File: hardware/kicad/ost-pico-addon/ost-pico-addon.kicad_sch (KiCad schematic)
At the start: 8 parts, among them J1 Conn_01x09_Male, J2 47219-2001, J3 buttons, J4 Conn_01x02_Pin, J5 Conn_01x07_Pin, U1 Pico

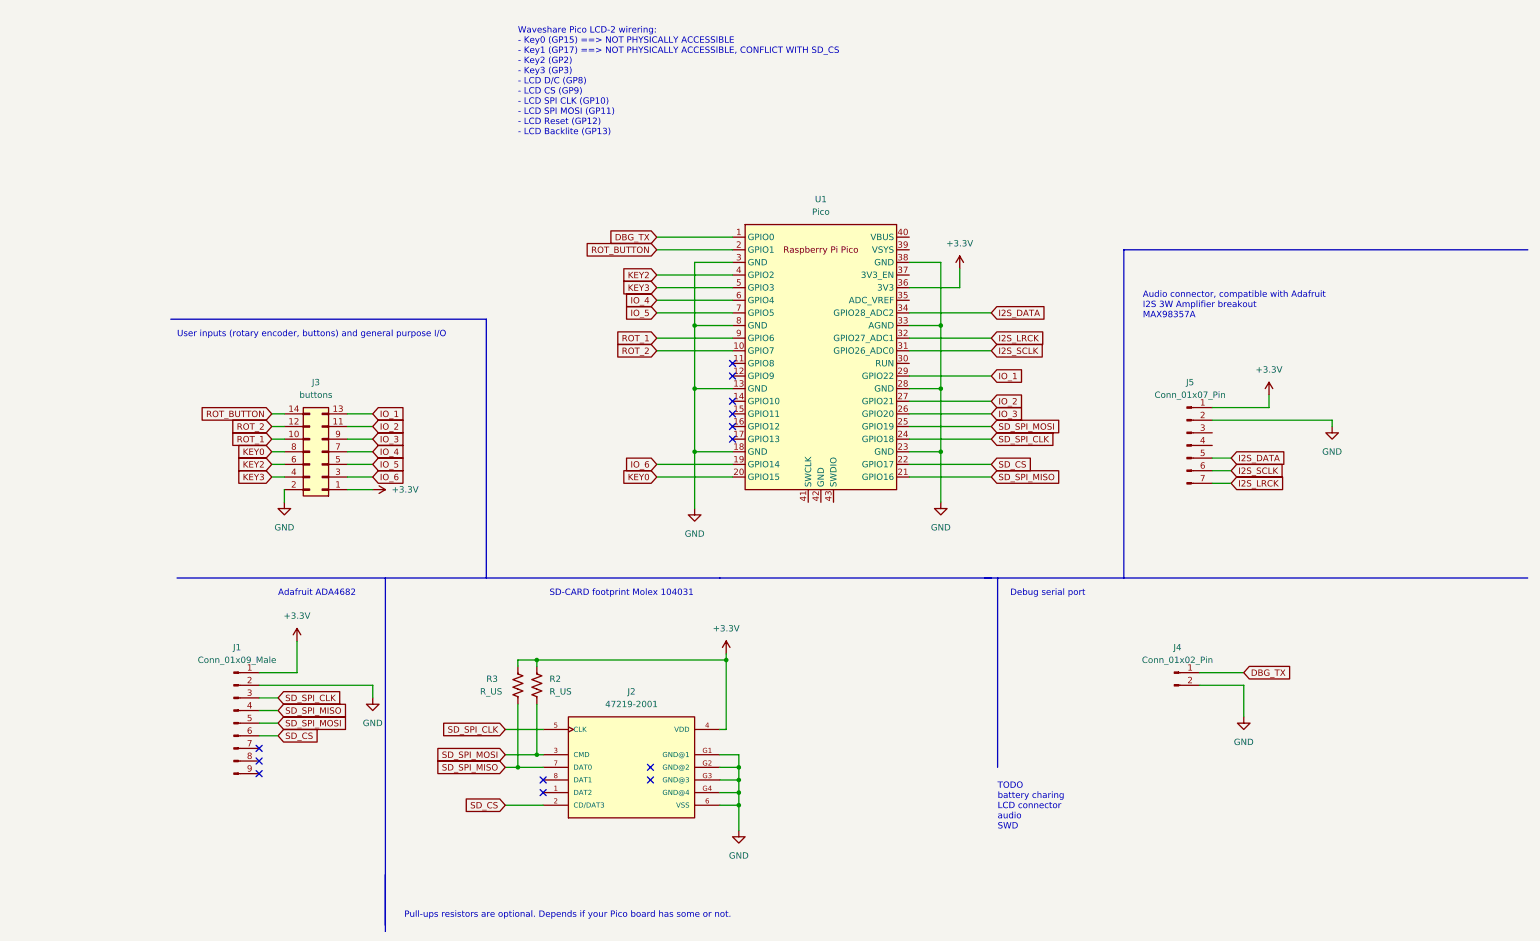
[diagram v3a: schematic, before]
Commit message: Pico audio with 3 audio chips (complex)
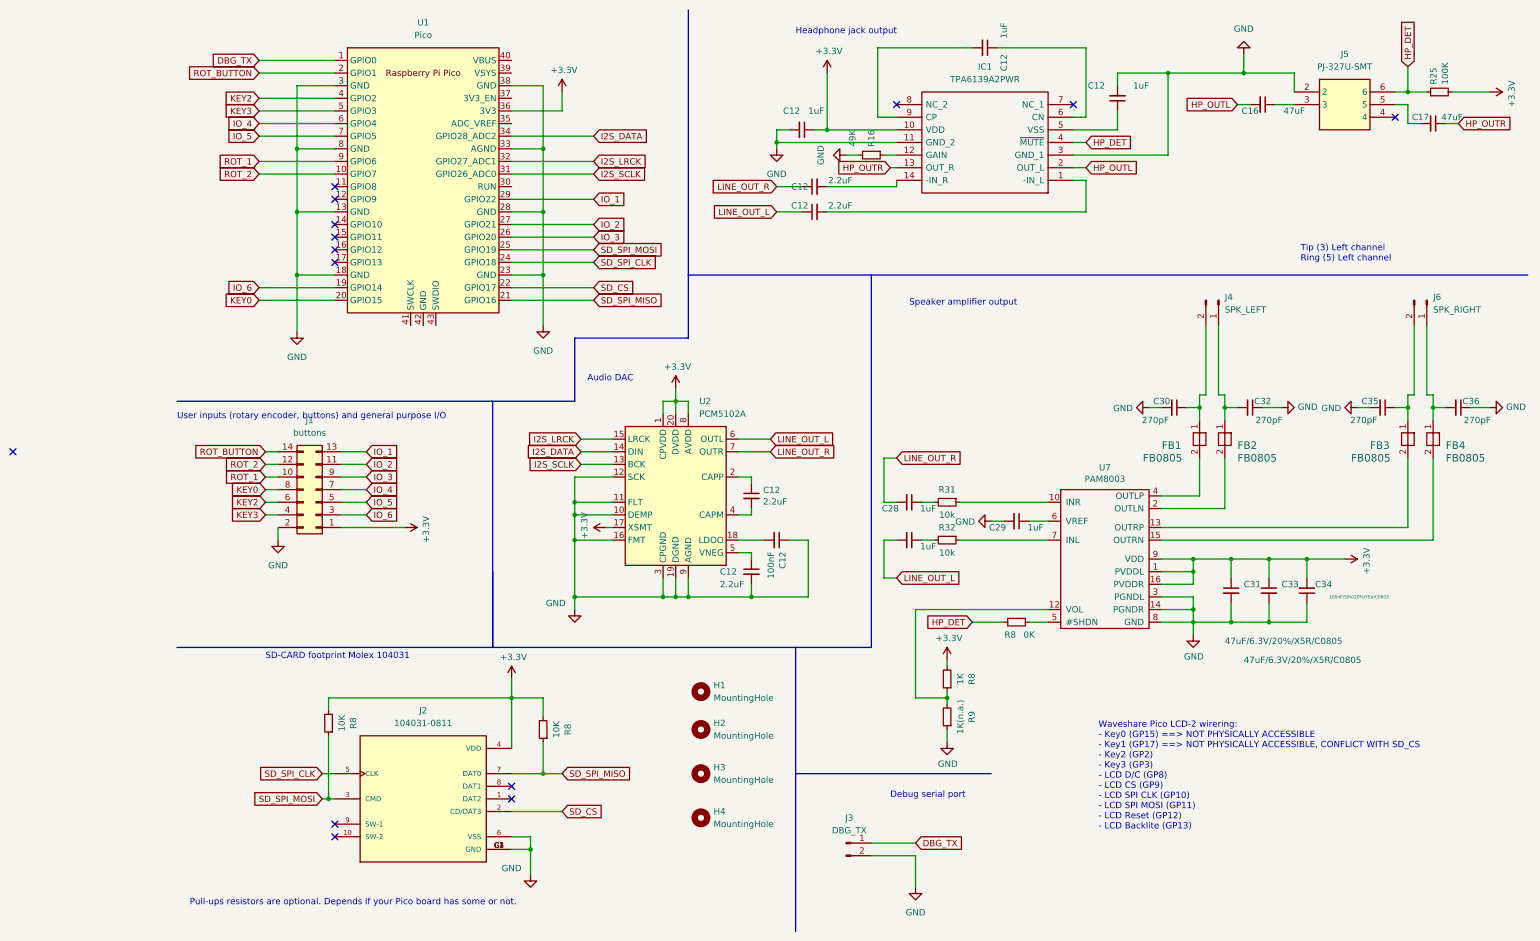
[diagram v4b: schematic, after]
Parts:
- removed J1: Conn_01x09_Male, Connector_PinHeader_2.54mm:PinHeader_1x09_P2.54mm_Vertical, symbol Connector:Conn_01x09_Male
- removed J2: 47219-2001, sdcard-libs:MOLEX_47219-2001, symbol sdcard-libs:47219-2001
- removed J5: Conn_01x07_Pin, Connector_PinHeader_2.54mm:PinHeader_1x07_P2.54mm_Vertical, symbol Connector:Conn_01x07_Pin
- removed R2, R3: R_US, Resistor_THT:R_Axial_DIN0207_L6.3mm_D2.5mm_P10.16mm_Horizontal, symbol Device:R_US
- added C12 (x4): 2.2uF, Capacitor_SMD:C_0805_2012Metric, symbol ESP32-ADF_Rev_C-rescue:C_Small-OLIMEX_RCL
- added C12 (x3), C27, C28, C29: 1uF, Capacitor_SMD:C_0805_2012Metric, symbol ESP32-ADF_Rev_C-rescue:C_Small-OLIMEX_RCL
- added C12: 100nF, Capacitor_SMD:C_0805_2012Metric, symbol ESP32-ADF_Rev_C-rescue:C_Small-OLIMEX_RCL
- added C16, C17: 47uF, Capacitor_SMD:C_0805_2012Metric, symbol ESP32-ADF_Rev_C-rescue:C_Small-OLIMEX_RCL
- added C30, C32, C35, C36: 270pF, Capacitor_SMD:C_0805_2012Metric, symbol ESP32-ADF_Rev_C-rescue:C_Small-OLIMEX_RCL
- added C31, C33: 47uF/6.3V/20%/X5R/C0805, Capacitor_SMD:C_0805_2012Metric, symbol ESP32-ADF_Rev_C-rescue:C-OLIMEX_RCL
- added C34: 100nF/50V/20%/Y5V/C0603, Capacitor_SMD:C_0805_2012Metric, symbol ESP32-ADF_Rev_C-rescue:C-OLIMEX_RCL
- added FB1, FB2, FB3, FB4: FB0805, Inductor_SMD:L_0805_2012Metric, symbol ESP32-ADF_Rev_C-rescue:FB0805-lz1ddd-ESP32-ADF_Rev_B-rescue
- added H1, H2, H3, H4: MountingHole, MountingHole:MountingHole_2.7mm_M2.5_ISO14580_Pad, symbol Mechanical:MountingHole
- added IC1: TPA6139A2PWR, audio:SOP65P640X120-14N, symbol TPA6139A2PWR:TPA6139A2PWR
- added J2: 104031-0811, sdcard-libs:MOLEX_104031-0811, symbol 104031-0811:104031-0811
- added J4: SPK_LEFT, Connector_PinHeader_2.54mm:PinHeader_1x02_P2.54mm_Vertical, symbol Connector:Conn_01x02_Pin
- added J5: PJ-327U-SMT, audio:PJ327USMT, symbol PJ-327U-SMT:PJ-327U-SMT
- added J6: SPK_RIGHT, Connector_PinHeader_2.54mm:PinHeader_1x02_P2.54mm_Vertical, symbol Connector:Conn_01x02_Pin
- added R16: 49K, Resistor_SMD:R_0805_2012Metric, symbol ESP32-ADF_Rev_C-rescue:R_Small-OLIMEX_RCL
- added R25: 100K, Resistor_SMD:R_0805_2012Metric, symbol ESP32-ADF_Rev_C-rescue:R_Small-OLIMEX_RCL
- added R31, R32: 10k, Resistor_SMD:R_0805_2012Metric, symbol ESP32-ADF_Rev_C-rescue:R_Small-OLIMEX_RCL
- added R8 (x2): 10K, Resistor_SMD:R_0805_2012Metric, symbol ESP32-ADF_Rev_C-rescue:R_Small-OLIMEX_RCL
- added R8: 0K, Resistor_SMD:R_0805_2012Metric, symbol ESP32-ADF_Rev_C-rescue:R_Small-OLIMEX_RCL
- added R8: 1K, Resistor_SMD:R_0805_2012Metric, symbol ESP32-ADF_Rev_C-rescue:R_Small-OLIMEX_RCL
- added R9: 1K(n.a.), Resistor_SMD:R_0805_2012Metric, symbol ESP32-ADF_Rev_C-rescue:R_Small-OLIMEX_RCL
- added U2: PCM5102A, Package_SO:TSSOP-20_4.4x6.5mm_P0.65mm, symbol Audio:PCM5102A
- added U7: PAM8003, audio:SO16, symbol ESP32-ADF_Rev_C-rescue:PAM8003-OLIMEX_IC-ESP32-ADF_Rev_B-rescue
- J3: renamed from J4; value Conn_01x02_Pin -> DBG_TX
- renumbered J3 to J1
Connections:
- net GND: now also C12.1, C12.2, C12.2, C12.2, C29.2, C30.2, C31.2, C32.1, C33.2, C34.1, C35.2, C36.1, IC1.11 (GND_2), IC1.3 (GND_1), J2.6 (VSS), J2.G1 (GND), J2.G2 (GND), J2.G3 (GND), J2.G4 (GND), J5.2, R16.2, R9.1, U2.10 (DEMP), U2.11 (FLT), U2.12 (SCK), U2.16 (FMT), U2.19 (DGND), U2.3 (CPGND), U2.9 (AGND), U7.14 (PGNDR), U7.3 (PGNDL), U7.8 (GND)
- net I2S_DATA: now also U2.14 (DIN)
- net I2S_LRCK: now also U2.15 (LRCK)
- net I2S_SCLK: now also U2.13 (BCK)
- net SD_CS: now also J2.2 (CD/DAT3)
- net SD_SPI_CLK: now also J2.5 (CLK)
- net SD_SPI_MISO: now also J2.7 (DAT0), R8.1
- net SD_SPI_MOSI: now also J2.3 (CMD), R8.1
- net +3.3V renamed +3V3
- net +3V3: now also C12.1, C31.1, C33.1, C34.2, IC1.10 (VDD), J2.4 (VDD), R25.2, R8.2, R8.2, R8.2, U2.1 (CPVDD), U2.17 (XSMT), U2.20 (DVDD), U2.8 (AVDD), U7.1 (PVDDL), U7.16 (PVDDR), U7.9 (VDD)
- new net: C12.2, IC1.14 (-IN_R)
- new net: C28.1, R32.2
- new net: C12.1, U2.5 (VNEG)
- new net: C36.2, FB4.1, J6.1 (Pin_1)
- new net: C35.1, FB3.1, J6.2 (Pin_2)
- new net: C30.1, FB1.1, J4.2 (Pin_2)
- new net: FB1.2, U7.4 (OUTLP)
- new net: R8.1, U7.5 (#SHDN)
- new net: C16.1, J5.3
- new net: C17.2, J5.5
- new net: IC1.12 (GAIN), R16.1
- new net: R8.1, R9.2, U7.12 (VOL)
- new net: C32.2, FB2.1, J4.1 (Pin_1)
- new net: R31.1, U7.7 (INL)
- new net: C27.1, R31.2
- new net: FB2.2, U7.2 (OUTLN)
- new net: R32.1, U7.10 (INR)
- new net: FB3.2, U7.13 (OUTRP)
- new net: FB4.2, U7.15 (OUTRN)
- new net: C29.1, U7.6 (VREF)
- new net: C12.1, IC1.6 (CN)
- new net: C12.2, IC1.9 (CP)
- new net: C12.2, U2.18 (LDOO)
- new net: C12.1, U2.2 (CAPP)
- new net: C12.2, U2.4 (CAPM)
- new net: C12.2, IC1.1 (-IN_L)
- new net: C12.1, IC1.5 (VSS)
- new net HP_DET: IC1.4 (~{MUTE}), J5.6, R25.1, R8.2
- new net HP_OUTL: C16.2, IC1.2 (OUT_L)
- new net HP_OUTR: C17.1, IC1.13 (OUT_R)
- new net LINE_OUT_L: C12.1, C27.2, U2.6 (OUTL)
- new net LINE_OUT_R: C12.1, C28.2, U2.7 (OUTR)
- no-connect marks 13 -> 14
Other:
- note added: "Audio DAC"
- note added: "Headphone jack output"
- note added: "Speaker amplifier output"
- note added: "Tip (3) Left channel Ring (5) Left channel"
- note removed: "Adafruit ADA4682"
- note removed: "Audio connector, compatible with Adafruit I2S 3W Amplifier breakout MAX98357A"
- note removed: "TODO battery charing LCD connector audio SWD"
- moved on the sheet: J1, J3, U1
